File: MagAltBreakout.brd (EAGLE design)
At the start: 49.5 x 39.4 mm, 0 parts

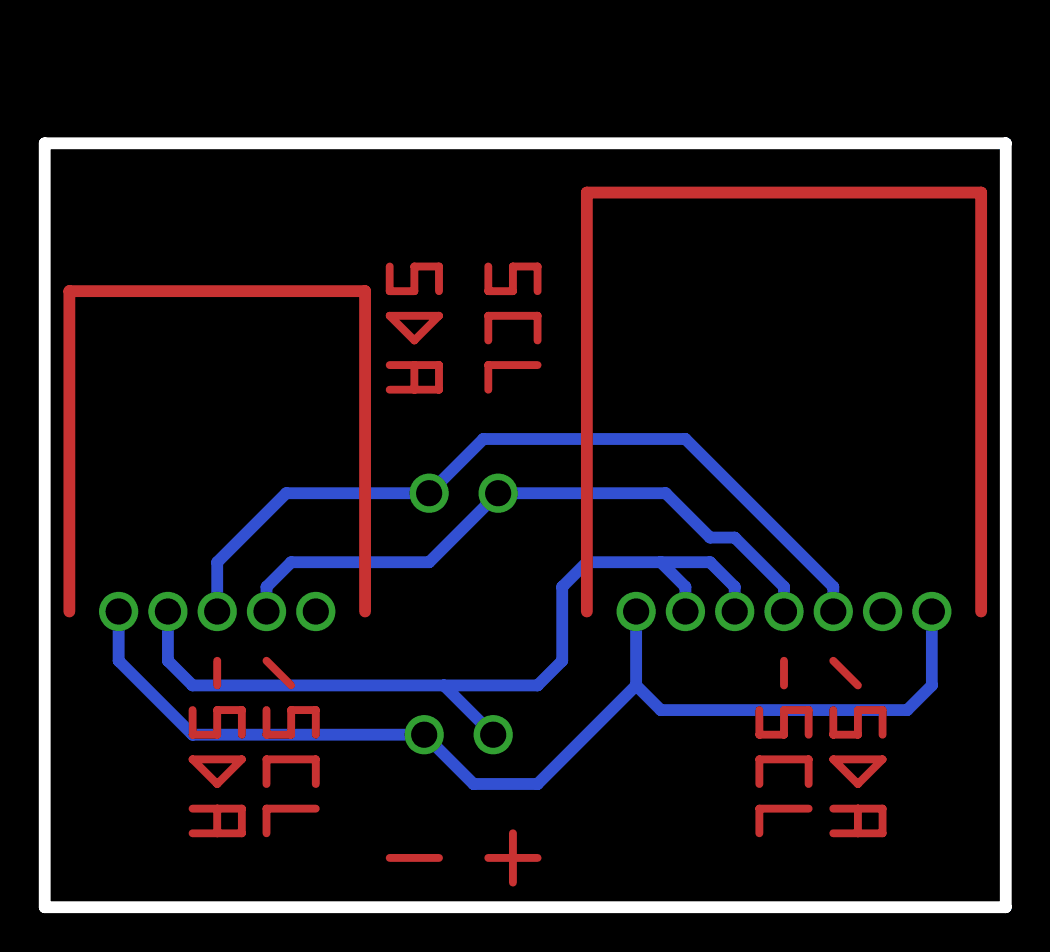
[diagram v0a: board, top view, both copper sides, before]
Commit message: Updated I2C board
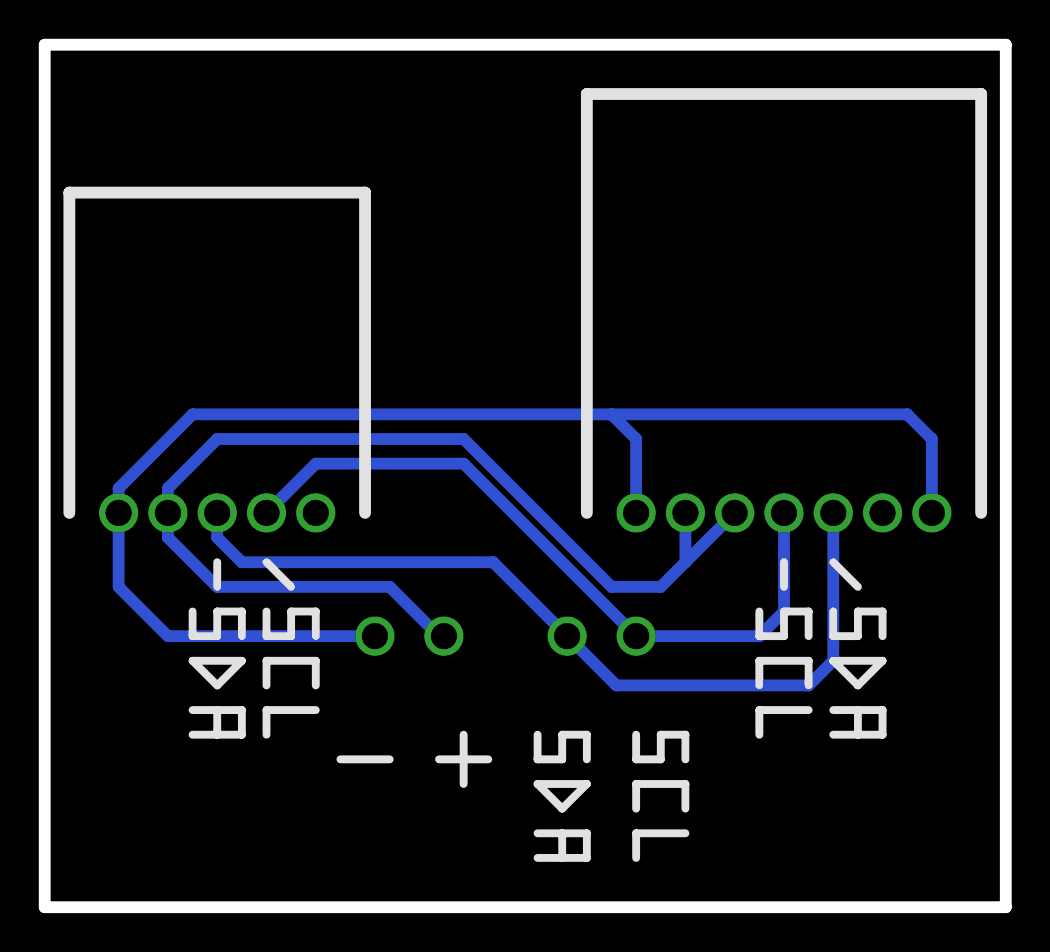
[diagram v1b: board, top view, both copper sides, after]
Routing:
- net S$1: track 63.5 -> 0.00 mm
- net S$2: track 48.3 -> 0.00 mm
- net GND: track 57.9 -> 72.8 mm
- net VCC: track 45.6 -> 56.4 mm
- net S$15: track 7.62 -> 0.00 mm
- net S$3: track 7.62 -> 0.00 mm
- net S$26: track 7.62 -> 0.00 mm
- net S$6: track 6.35 -> 0.00 mm
- net S$5: track 6.35 -> 0.00 mm
- net S$16: track 6.35 -> 0.00 mm
- net S$12: track 6.35 -> 0.00 mm
- net S$24: track 6.35 -> 0.00 mm
- net S$21: track 6.35 -> 0.00 mm
- net S$13: track 6.13 -> 0.00 mm
- net S$25: track 6.13 -> 0.00 mm
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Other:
- board size 49.5 x 39.4 mm -> 49.5 x 44.5 mm
